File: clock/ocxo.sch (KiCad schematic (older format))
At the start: 45 parts, among them Q201 MMBT3904, U201 PCA9306, U202 DAC8830, U203 LMV722, U204 LTC2990, U205 LP3853, U206 NC7SZ125, U207 NC7SZ125, Y201 FVXO-HC53, Y202 CX210

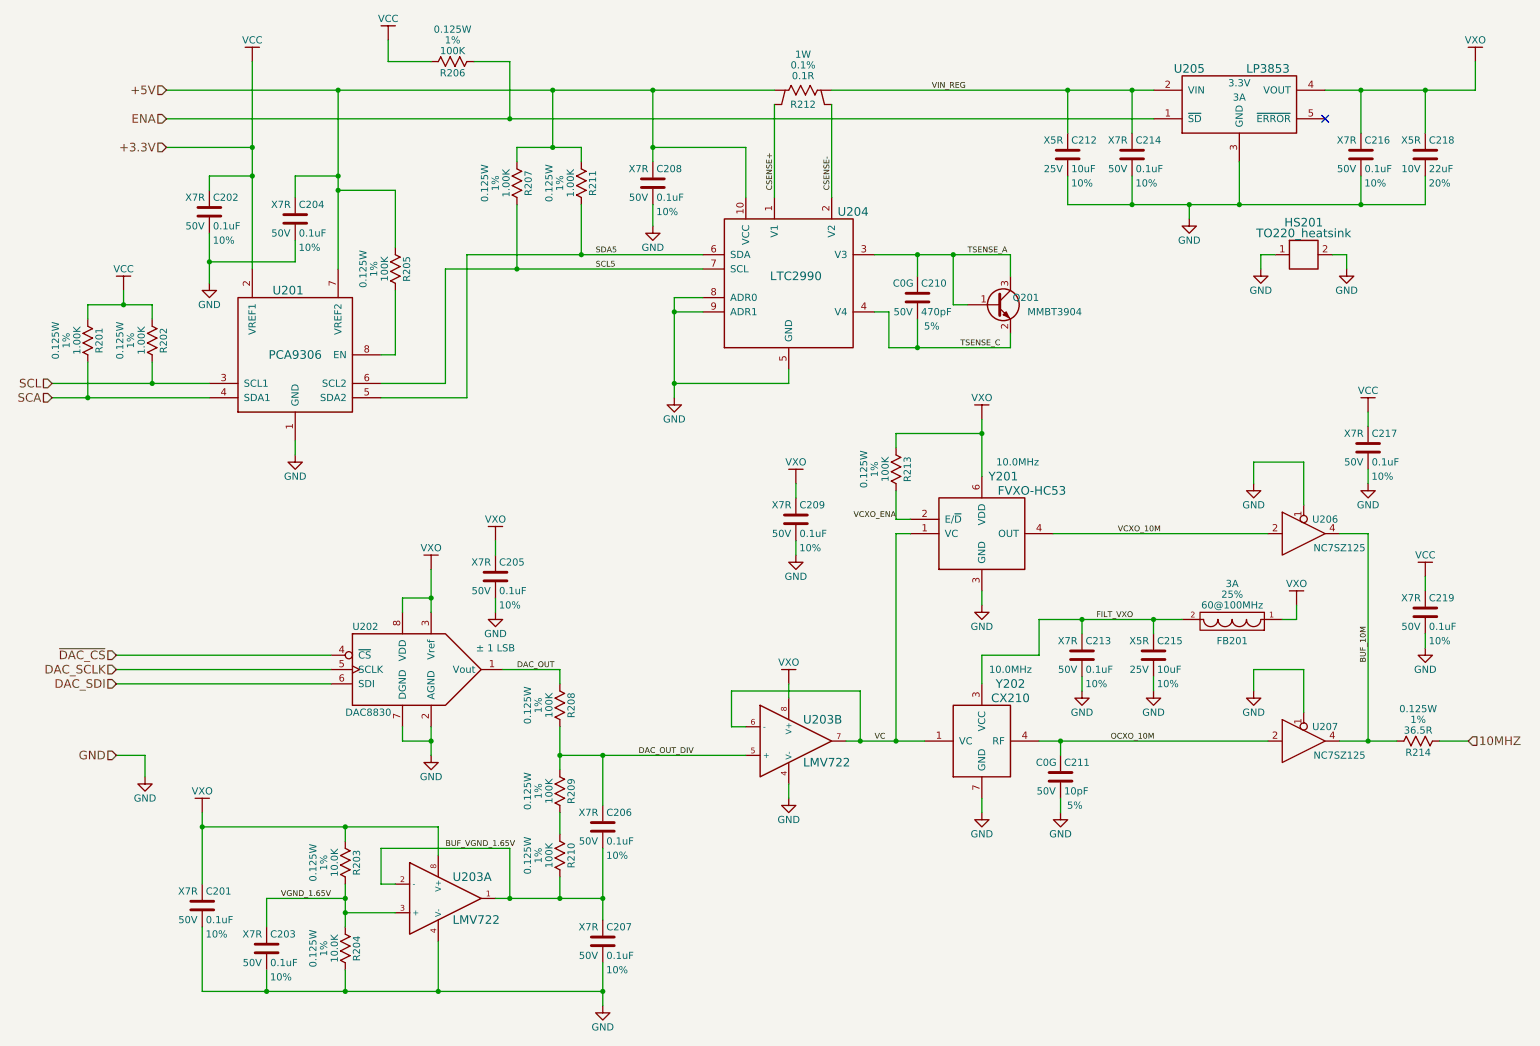
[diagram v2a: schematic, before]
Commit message: Clean up most of the schematic DRC errors. Update placement.
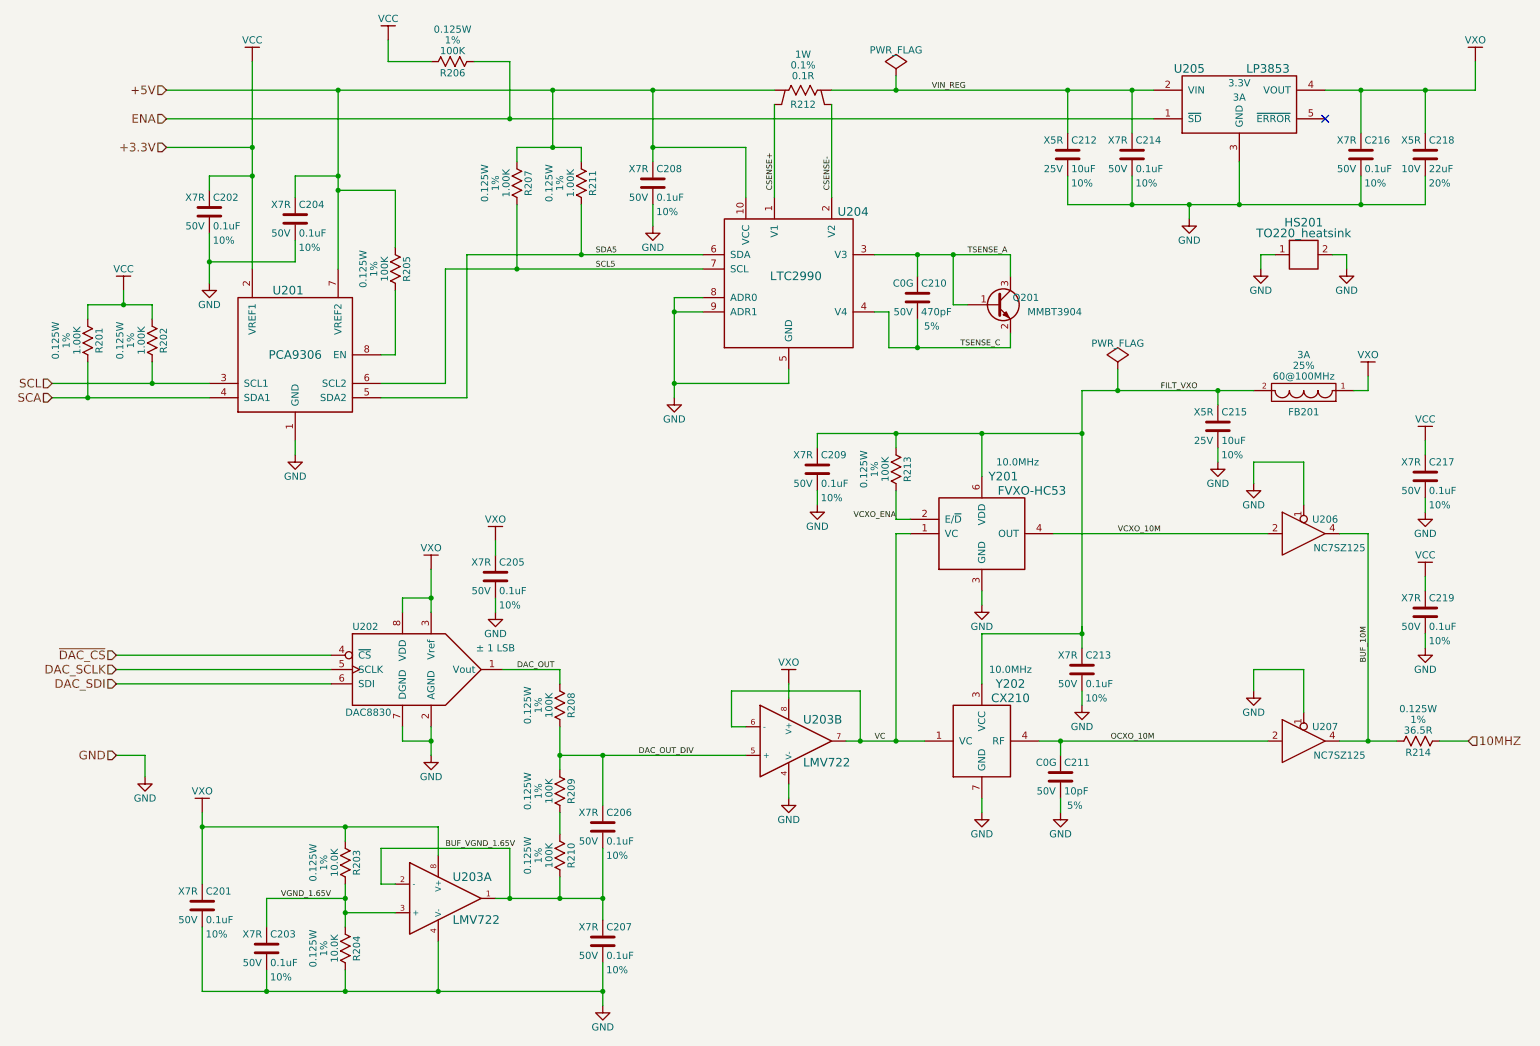
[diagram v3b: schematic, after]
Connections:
- net FILT_VXO: now also C209.1, R213.1, Y201.6 (VDD)
- net VXO: no longer C209.1, R213.1, Y201.6 (VDD)
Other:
- moved on the sheet: C209, C213, C215, C217, FB201

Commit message: Checkpoint PCB placement.
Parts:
- added A201: CX210_Cover, local:CX210_Cover, symbol CX210_Cover
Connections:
- net LV_ENA: now reaches R205.2, U201.8 (EN)
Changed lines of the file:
@@
 Connection ~ 6750 3550
 Connection ~ 8050 4950
+$Comp
+L CX210_Cover A201
+U 1 1 56459BA1
+P 8800 6150
+F 0 "A201" H 8800 6350 60  0000 C CNN
+F 1 "CX210_Cover" H 8800 6200 50  0000 C CNN
+F 2 "local:CX210_Cover" H 8700 6250 60  0001 C CNN
+F 3 "" H 8800 6350 60  0000 C CNN
+F 4 "Custom" H 8800 6500 50  0001 C CNN "Manufacturer"
+F 5 "PN" H 8800 6425 50  0001 C CNN "PartNum"
+	1    8800 6150
+	1    0    0    -1
+$EndComp
+Text Label 3250 2900 1    40   ~ 0
+LV_ENA
 $EndSCHEMATC

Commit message: Correct spelling. Minor clean ups.
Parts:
- Q201: Manufacturer (none) -> NXP Semiconductors
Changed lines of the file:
@@
 F 2 "Housings_SOT-23_SOT-143_TSOT-6:SOT-23_Handsoldering" H 7650 2750 29  0001 C CNN
 F 3 "" H 7450 2650 60  0000 C CNN
-F 4 "MMBT3904" H 7850 2500 50  0001 C CNN "PartNum"
+F 4 "NXP Semiconductors" H 7450 2650 50  0001 C CNN "Manufacturer"
+F 5 "MMBT3904" H 7850 2500 50  0001 C CNN "PartNum"
 	1    7450 2650
 	1    0    0    -1

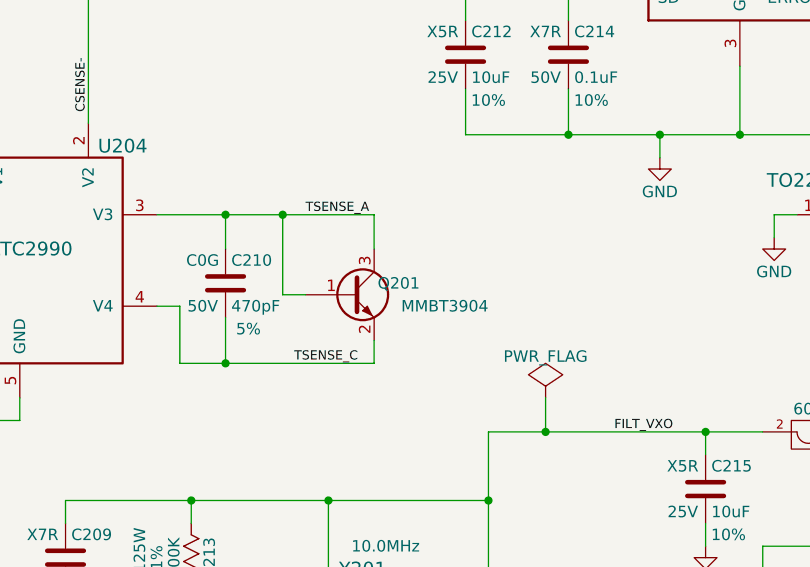
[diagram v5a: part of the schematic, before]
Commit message: Change SOT-23 footprint. Move some vias onto grid.
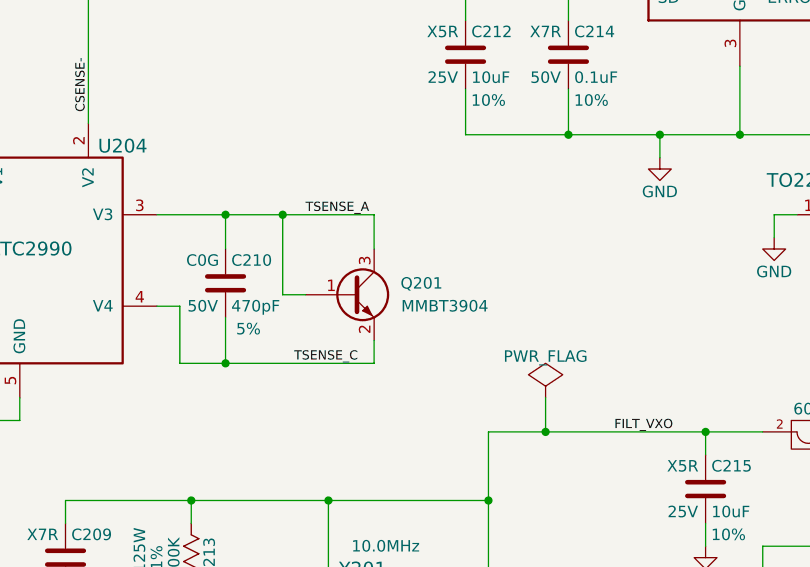
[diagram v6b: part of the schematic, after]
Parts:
- Q201: footprint Housings_SOT-23_SOT-143_TSOT-6:SOT-23_Handsoldering -> local:SOT-23-3_NXP_HandSoldering
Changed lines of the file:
@@
 U 1 1 562FC26B
 P 7450 2650
-F 0 "Q201" H 7750 2700 50  0000 R CNN
+F 0 "Q201" H 7850 2700 50  0000 R CNN
 F 1 "MMBT3904" H 8050 2600 50  0000 R CNN
-F 2 "Housings_SOT-23_SOT-143_TSOT-6:SOT-23_Handsoldering" H 7650 2750 29  0001 C CNN
+F 2 "local:SOT-23-3_NXP_HandSoldering" H 7650 2750 29  0001 C CNN
 F 3 "" H 7450 2650 60  0000 C CNN
 F 4 "NXP Semiconductors" H 7450 2650 50  0001 C CNN "Manufacturer"

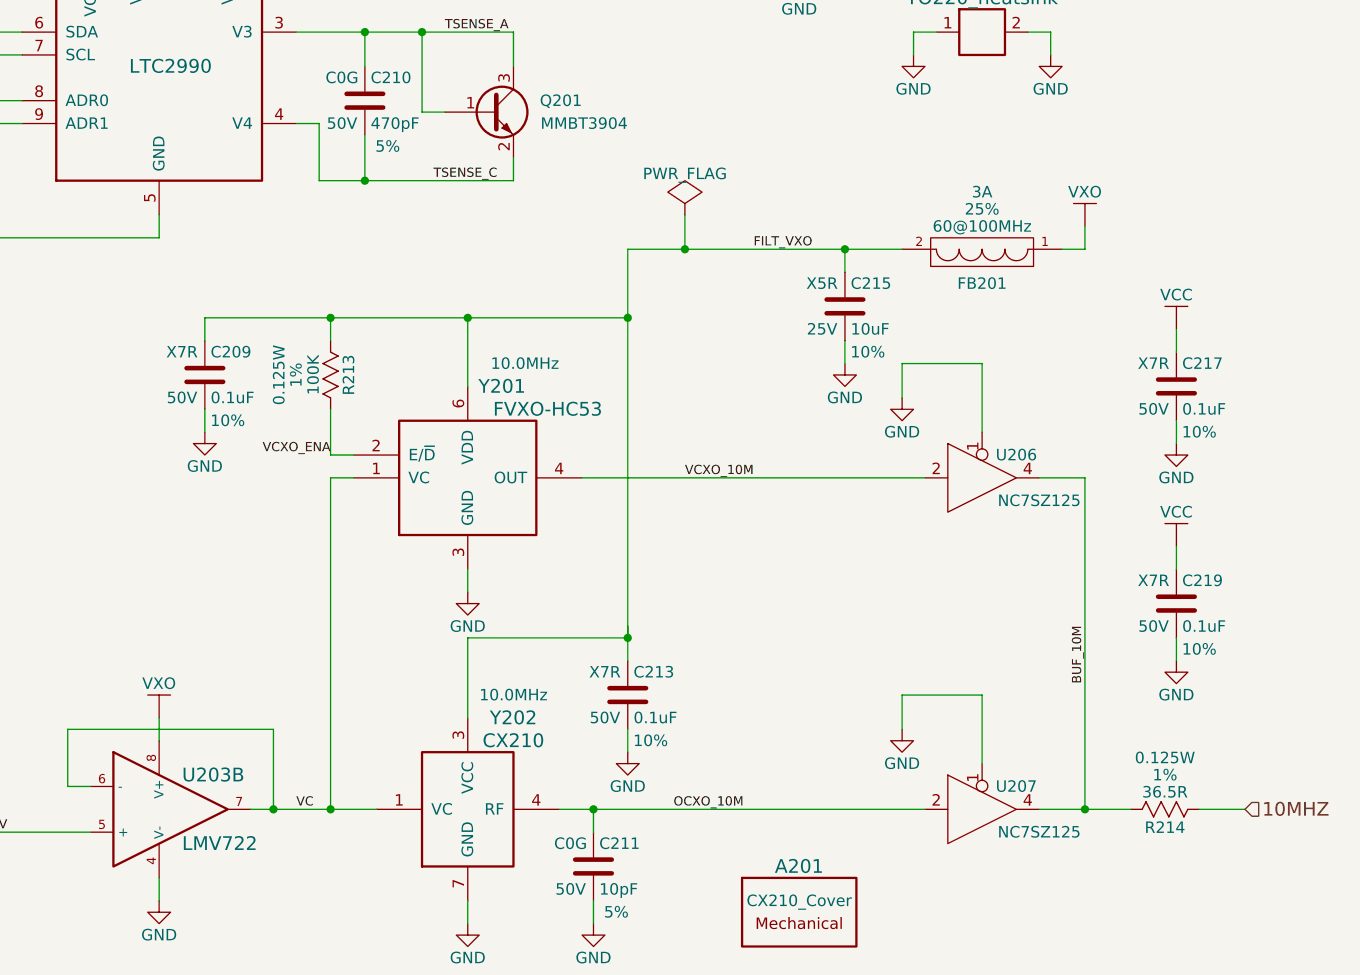
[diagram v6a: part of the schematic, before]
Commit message: Lock all the stitching vias. Remove FVXO alternate to OCXO.
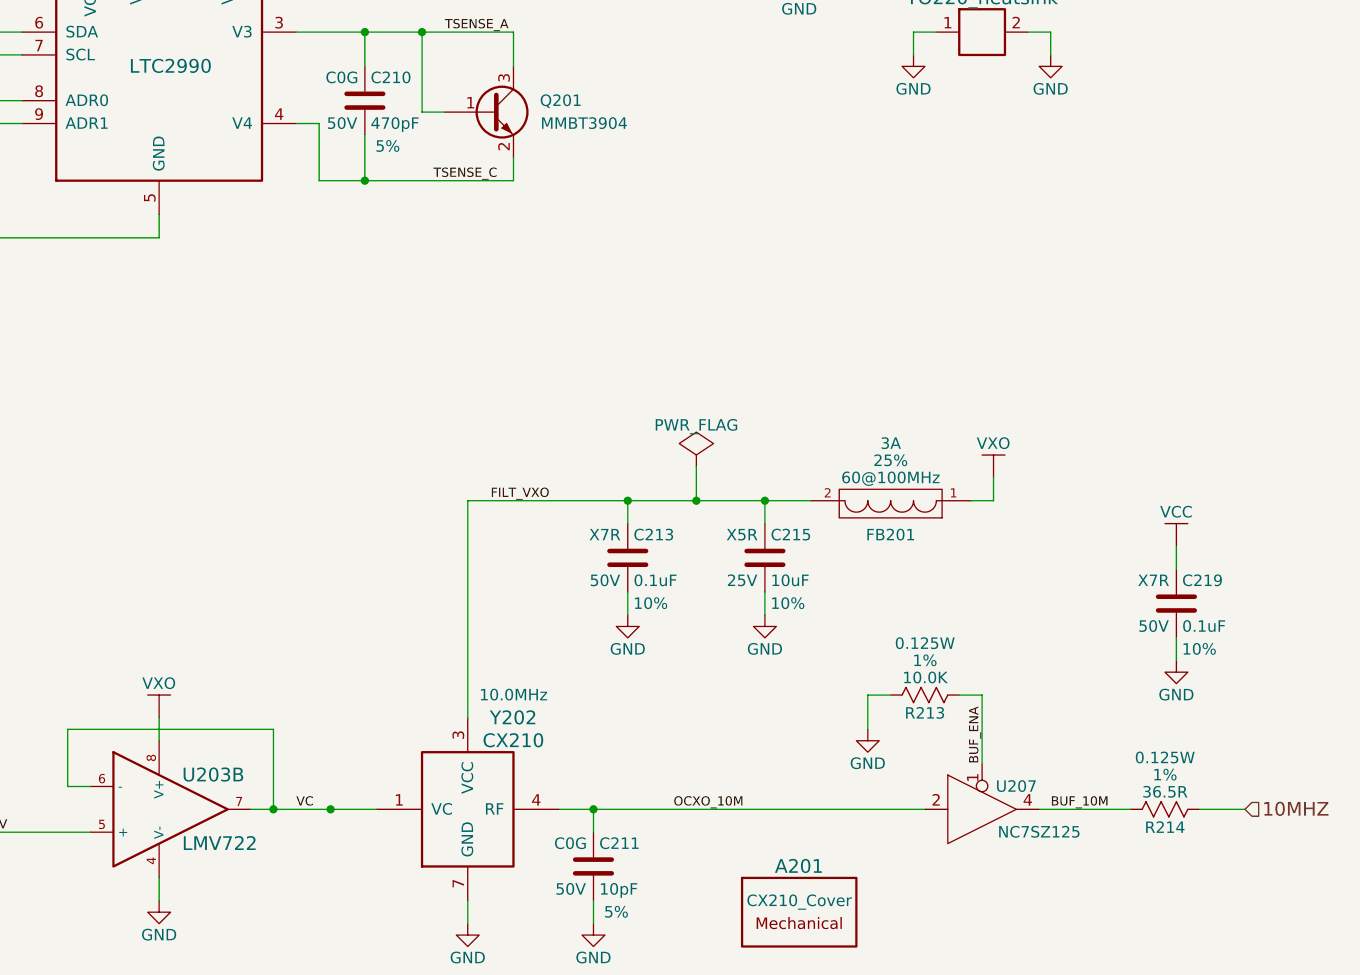
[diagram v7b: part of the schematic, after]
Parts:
- removed C209, C217: 0.1uF, Capacitors_SMD:C_0805_HandSoldering, symbol C
- removed U206: NC7SZ125, local:SOT-23-5_1.6x2.9mm_Pitch0.95mm, symbol NC7SZ125
- removed Y201: FVXO-HC53, local:FVXO_HandSoldering, symbol FVXO-HC53
- R213: value 100K -> 10.0K; PartNum CRCW0805100KFKEA -> CRCW080510K0FKEA
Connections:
- net VCXO_ENA is gone; now on net GND: R213.2
- net FILT_VXO: no longer R213.1
- net GND: no longer U207.1
- new net BUF_ENA: R213.1, U207.1
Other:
- moved on the sheet: C213, C215, FB201
